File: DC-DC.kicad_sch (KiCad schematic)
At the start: 4 parts, among them U5 CRE1S0505S3C

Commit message: Assign footprints to devices
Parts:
- C1, C2, C3: footprint (none) -> Capacitor_SMD:C_0201_0603Metric
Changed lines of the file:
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@@
 			)
 		)
-		(property "Footprint" ""
+		(property "Footprint" "Capacitor_SMD:C_0201_0603Metric"
 			(at 77.47 55.88 0)
 			(effects
@@
 			)
 		)
-		(property "Footprint" ""
+		(property "Footprint" "Capacitor_SMD:C_0201_0603Metric"
 			(at 150.8252 60.96 0)
 			(effects
@@
 			)
 		)
-		(property "Footprint" ""
+		(property "Footprint" "Capacitor_SMD:C_0201_0603Metric"
 			(at 130.81 57.15 0)
 			(effects

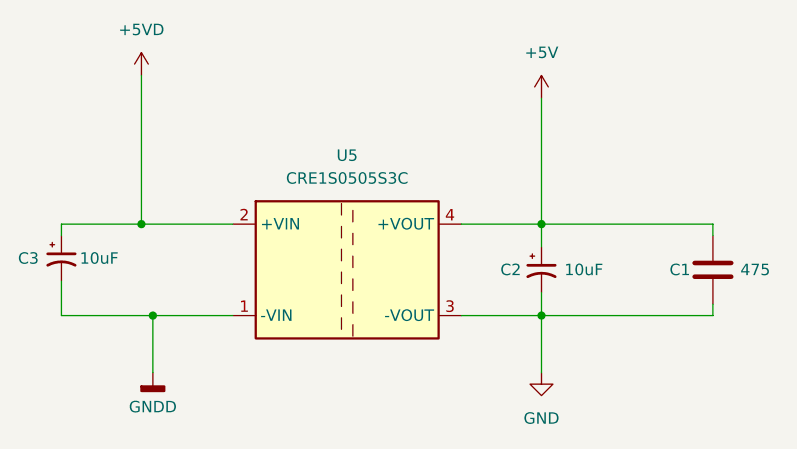
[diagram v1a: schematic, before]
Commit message: Move Radio interface onto it's own sheet, Add mounting holes and case outline
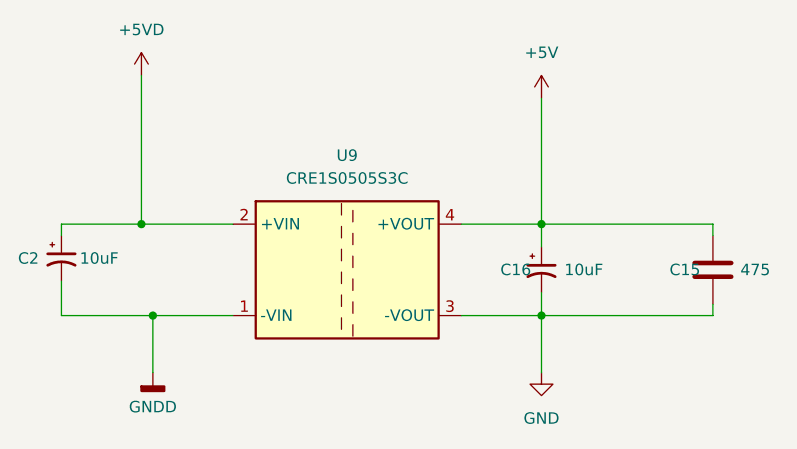
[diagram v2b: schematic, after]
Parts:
- renumbered C1 to C15, C2 to C16, C3 to C2, U5 to U9
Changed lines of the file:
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@@
 		(on_board yes)
 		(dnp no)
-		(property "Reference" "C3"
+		(property "Reference" "C2"
 			(at 72.644 55.88 0)
 			(effects
@@
 			(project "digital-mode-radio-interface"
 				(path "/a0d4bcf6-6cac-4e92-853e-9083f008b231/aacc300d-671a-4923-bc80-280628078a5d"
-					(reference "C3")
+					(reference "C2")
 					(unit 1)
 				)
@@
 		(on_board yes)
 		(dnp no)
-		(property "Reference" "C1"
+		(property "Reference" "C15"
 			(at 145.034 57.15 0)
 			(effects
@@
 			(project "digital-mode-radio-interface"
 				(path "/a0d4bcf6-6cac-4e92-853e-9083f008b231/aacc300d-671a-4923-bc80-280628078a5d"
-					(reference "C1")
+					(reference "C15")
 					(unit 1)
 				)
@@
 		(on_board yes)
 		(dnp no)
-		(property "Reference" "C2"
+		(property "Reference" "C16"
 			(at 126.238 57.15 0)
 			(effects
@@
 			(project "digital-mode-radio-interface"
 				(path "/a0d4bcf6-6cac-4e92-853e-9083f008b231/aacc300d-671a-4923-bc80-280628078a5d"
-					(reference "C2")
+					(reference "C16")
 					(unit 1)
 				)
@@
 		(dnp no)
 		(fields_autoplaced yes)
-		(property "Reference" "U5"
+		(property "Reference" "U9"
 			(at 109.22 44.45 0)
 			(effects
@@
 			(project "digital-mode-radio-interface"
 				(path "/a0d4bcf6-6cac-4e92-853e-9083f008b231/aacc300d-671a-4923-bc80-280628078a5d"
-					(reference "U5")
-					(unit 1)
-				)
+					(reference "U9")
+					(unit 1)
+				)

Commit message: kiCAD 9.0
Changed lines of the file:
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@@
 (kicad_sch
-	(version 20231120)
+	(version 20250114)
 	(generator "eeschema")
-	(generator_version "8.0")
+	(generator_version "9.0")
 	(paper "USLetter")
 	(title_block
